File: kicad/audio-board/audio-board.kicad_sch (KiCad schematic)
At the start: 45 parts, among them J1 TO_CM5, J2 VBAT_IN, U1 ADAU1861, U10 ADP7118AUJZ-3.3-R7, U2 ADXL354CEZ, U3 LTC6242, U4 IM72D128VV01, U5 AD2428WBCPZ, U6 SN74LVC8T245PWR, U7 SN74LVC8T245PWR, U8 PCA9517ADP, U9 ADP7118AUJZ-1.8-R7

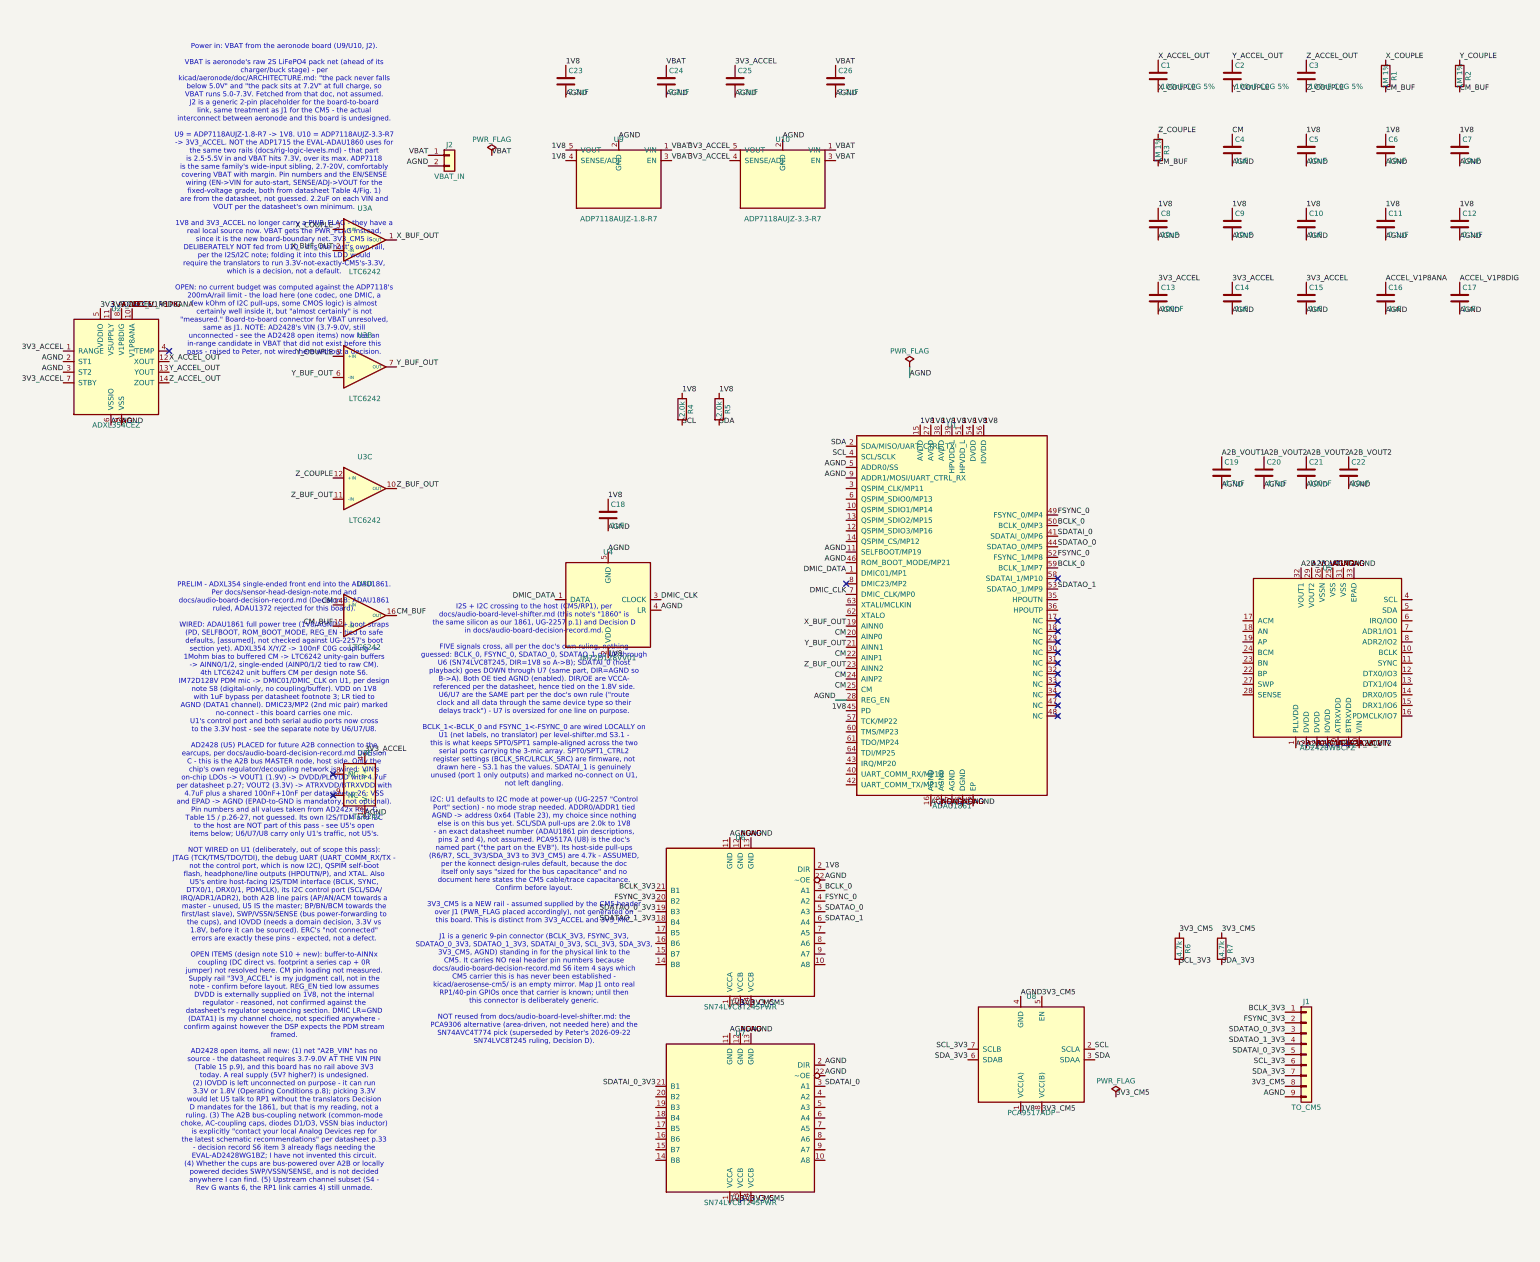
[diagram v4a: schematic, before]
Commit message: [LIMA] wire AD2428's VIN to VBAT, per Peter - closes the open supply gap
VBAT (5.0-7.3V, aeronode's raw 2S LiFePO4 pack) sits inside the AD2428's 3.7-9.0V VIN requirement
(AD242x Rev. C Table 15) with margin at both ends, so U5's VIN now ties directly to the same VBAT
net that feeds U9/U10. Removed the now-stale "A2B_VIN has no source" open item and the single-pin
label that went with it. AD2428's own on-chip VOUT1/VOUT2 regulators are unchanged - this only
supplies their input.

Design notes updated: the AD2428 note's open-items list drops the VIN gap, and the power note
records the connection and flags one thing not checked - no transient/inrush analysis for three
loads (U9, U10, U5's internal regulator) sharing one VBAT feed through J2.
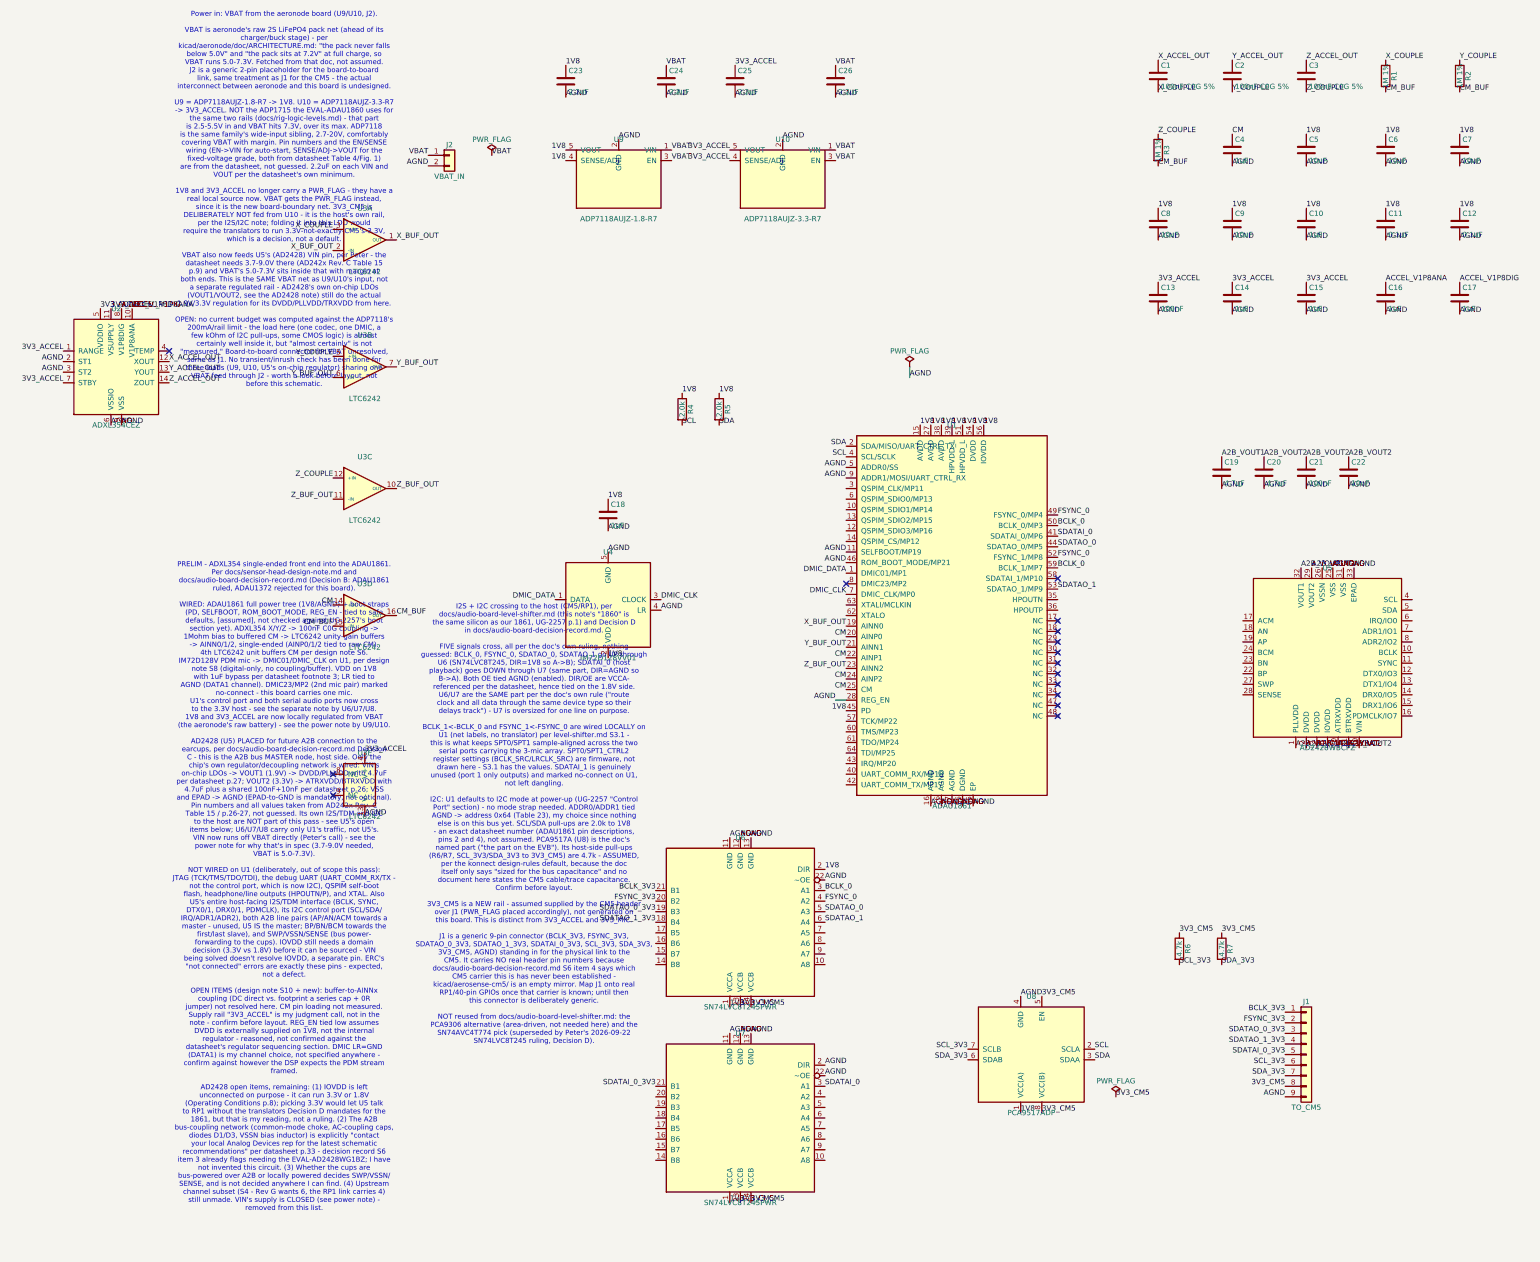
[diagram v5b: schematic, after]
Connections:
- net A2B_VIN is gone; now on net VBAT: U5.30 (VIN)

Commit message: [LIMA] AD2428 shares ADAU1861's I2C bus, per Peter - no new translator or pull-ups needed
U5's SCL/SDA now tie to the same SCL/SDA nets as U1, sharing the existing 2.0k pull-ups to 1V8
and the existing PCA9517A (U8) repeater to the host - I2C is multi-drop by design, so this needed
no new hardware. IOVDD -> 1V8 as a direct consequence: the AD242x datasheet warns operation isn't
guaranteed above VI2C_VBUS, and this bus's pull-ups sit at 1.8V, so U5 has to run its digital I/O
at the same rail to be a valid node on it - this also closes the "IOVDD domain" open item that was
sitting unresolved since the AD2428 was first placed. ADR1/ADR2 tied AGND (defined, non-floating
strap, matching how U1's own ADDR0/ADDR1 were handled) to give U5 a distinct base address per the
datasheet's multi-master-on-one-bus mechanism - flagged as a new open item that the resulting 7-bit
address isn't confirmed, since that table lives in a separate Technical Reference not in this repo.

Design notes updated: the I2S/I2C note explains the sharing and why IOVDD followed from it; the
main note's AD2428 open-items list drops VIN and IOVDD (both closed) and adds the I2C address
confirmation gap.
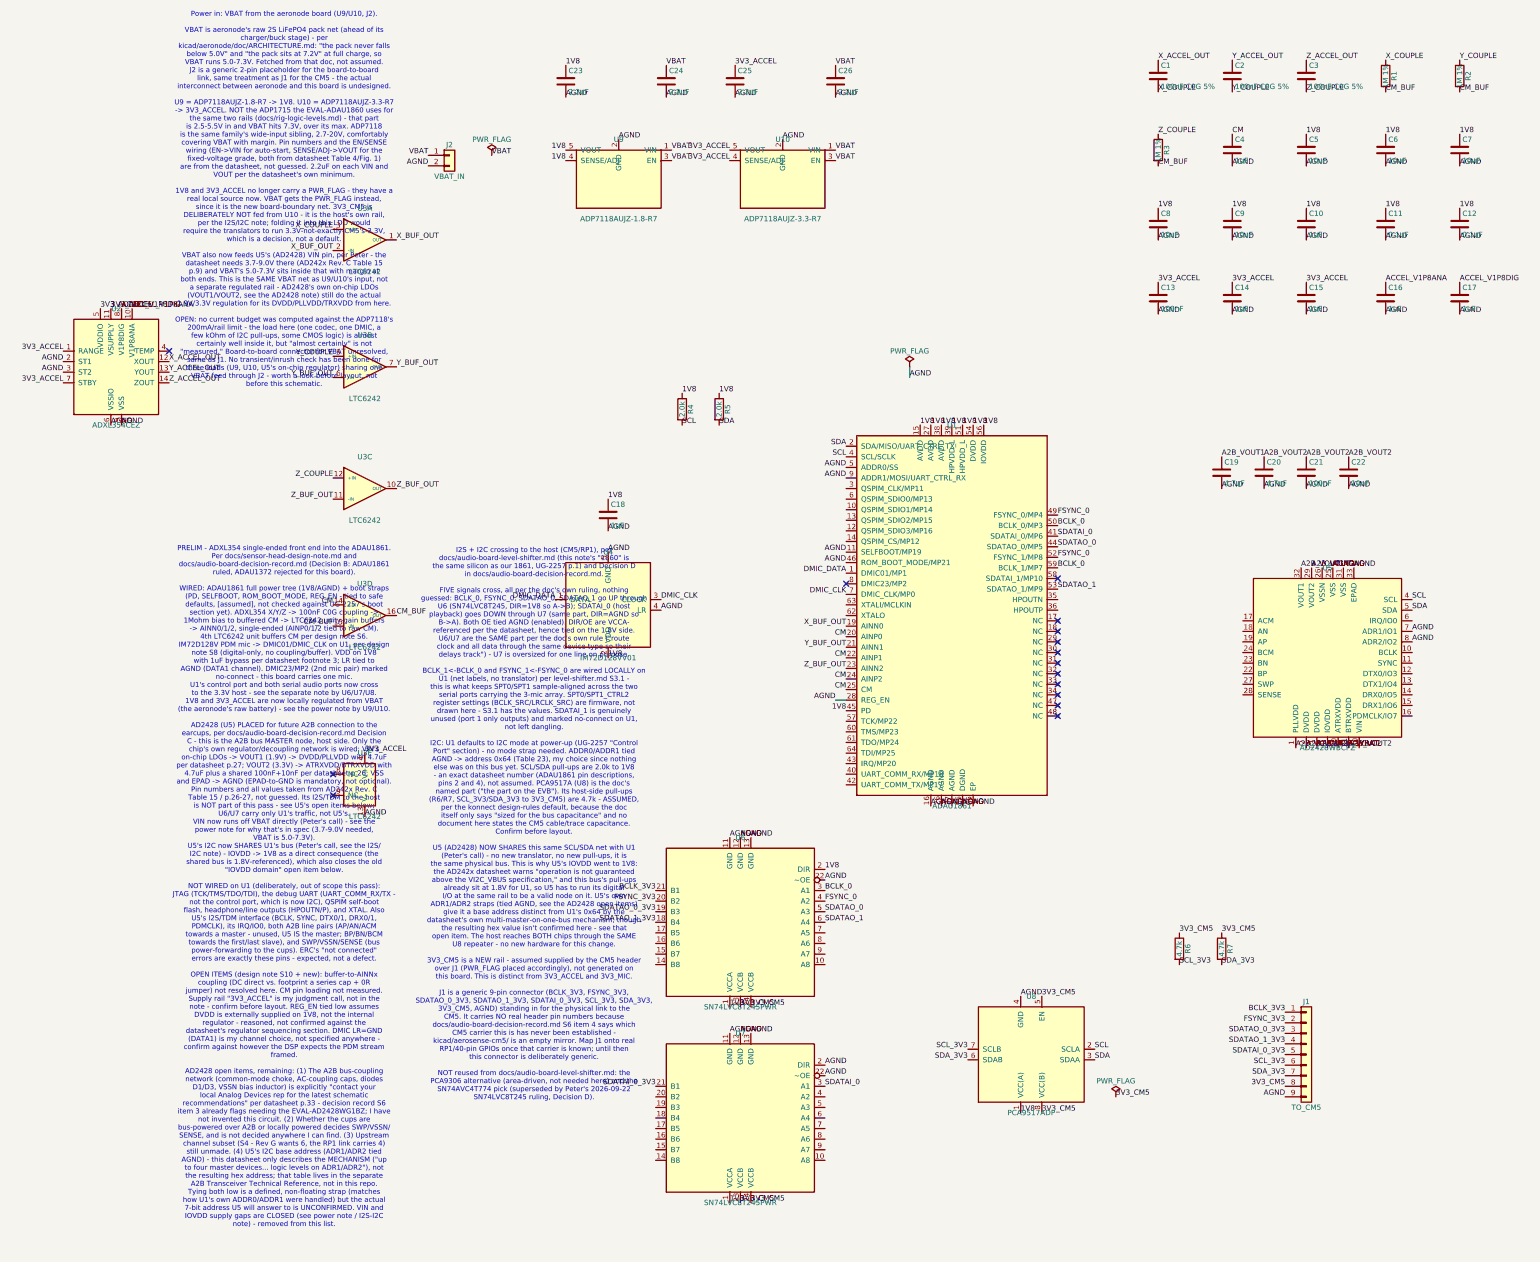
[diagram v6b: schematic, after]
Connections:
- net 1V8: now also U5.9 (IOVDD)
- net AGND: now also U5.7 (ADR1/IO1), U5.8 (ADR2/IO2)
- net SCL: now also U5.4 (SCL)
- net SDA: now also U5.5 (SDA)

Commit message: [LIMA] reroute U1's SPT1 from the host to AD2428's DRX1/DTX1, per Peter
SDATAO_1 (codec TX, mic3 data) -> U5 DRX1/IO6 (AD2428 RX); SDATAI_1 (codec RX) <- U5 DTX1/IO4
(AD2428 TX) - the correct TX/RX crossover. This replaces SPT1's old path to the host: removed
SDATAO_1 from U6 (A4/B4) and SDATAO_1_3V3 from J1 pin 4, and removed the no-connect that had been
on SDATAI_1 (it's a real signal now, not genuinely unused). No translator needed for this hop -
U5's IOVDD is already 1V8 (set when its I2C was put on U1's shared bus), so SPT1-to-AD2428 is a
native 1.8V link.

Flagged, not silently resolved: U5's BCLK/SYNC are still unconnected, and the decision record's
assumption that "RP1 drives them" no longer obviously holds now that DRX1/DTX1 exchange data with
U1's SPT1 - SPT1's own BCLK_1/FSYNC_1 are looped back from SPT0, not sourced from RP1. Wiring U5's
BCLK/SYNC to anything without settling which clock domain it should live in would guess at an
architecture decision, so I left it explicit in the I2S/I2C note as an open question with the two
live options named. Also flagged: mic3's data has no path to RP1 until DTX0/DTX1 and BCLK/SYNC are
wired, which doesn't exist yet - worth confirming that's the intended interim state.
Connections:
- net SDATAO_1: now also U5.15 (DRX1/IO6); no longer U6.6 (A4)
- net SDATAI_1: now reaches U5.13 (DTX1/IO4)
- net SDATAI_1: now also U1.58 (SDATAI_1/MP10)
- net SDATAO_1_3V3: no longer names the net of J1.4 (Pin_4)
- net SDATAO_1_3V3: no longer U6.18 (B4)
- no-connect marks 15 -> 14
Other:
- note added: "I2S + I2C crossing to the host (CM5/RP1), per docs/audio-board-level-shifter.md (this note's "1860" is the same silicon as our 1861, UG-2257 p.1) and Decision D in docs/audio-board-decision-record.md. FOUR signals cross to the host now (was five - see SPT1 below): BCLK_0, FSYNC_0, SDATAO_0 go UP through U6 (SN74LVC8T245, DIR=1V8 so A->B); SDATAI_0 (host playback) goes DOWN through U7 (same part, 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"
- note removed: "I2S + I2C crossing to the host (CM5/RP1), per docs/audio-board-level-shifter.md (this note's "1860" is the same silicon as our 1861, UG-2257 p.1) and Decision D in docs/audio-board-decision-record.md. FIVE signals cross, all per the doc's own ruling, nothing guessed: BCLK_0, FSYNC_0, SDATAO_0, SDATAO_1 go UP through U6 (SN74LVC8T245, DIR=1V8 so A->B); SDATAI_0 (host playback) goes DOWN through U7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"

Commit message: [LIMA] loop BCLK_1/FSYNC_1 to U5's BCLK/SYNC too, per Peter - closes the SPT1 clock-domain gap
U5's BCLK/SYNC (pins 10, 11) now tie to the same BCLK_0/FSYNC_0 nets that already loop into U1's
own BCLK_1/FSYNC_1 (level-shifter.md S3.1). U1 is now the single clock source for SPT0, SPT1, and
U5's local I2S/TDM port - resolving the gap flagged last pass: U5's DRX1/DTX1 exchange data with
SPT1 on a clock both sides actually share, instead of the originally-assumed "RP1 drives U5's
BCLK/SYNC," which would have left DRX1/DTX1 framed against a clock domain SPT1 was never on.

Consequence worth keeping visible, and called out explicitly in the I2S/I2C note rather than
glossed over: U5's I2S/TDM port is now fully local to this board. It no longer exchanges data with
RP1 at all. Whatever RP1 is meant to get from U5 (mic3, ultimately) has to cross the A2B bus and
come back out DTX0/DTX1 on their own separate, still-unbuilt link to RP1 - not "the same wires as
before." Flagged as the thing to confirm before assuming mic3 reaches the host in this design.

Design notes updated: the AD2428 open-items list drops the clock-domain question (closed) and
sharpens the still-open "mic3 has no path to RP1 yet" item with why that's now true.
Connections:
- net BCLK_0: now also U5.10 (BCLK)
- net FSYNC_0: now also U5.11 (SYNC)
